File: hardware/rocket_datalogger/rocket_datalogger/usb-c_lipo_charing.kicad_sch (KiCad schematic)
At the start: 11 parts, among them J3 JST-PH 1x2, U3 MCP73831-2-OT

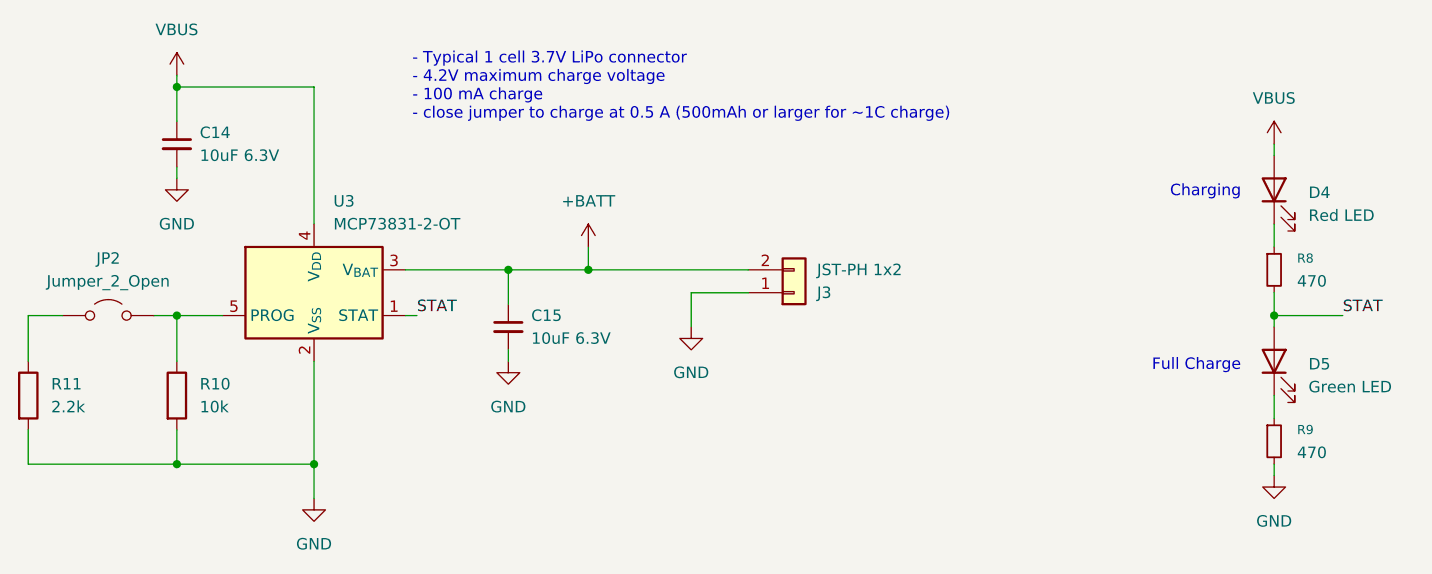
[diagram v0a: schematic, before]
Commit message: Changed IMU to BNO055
Previous IMU required 1.85V rail
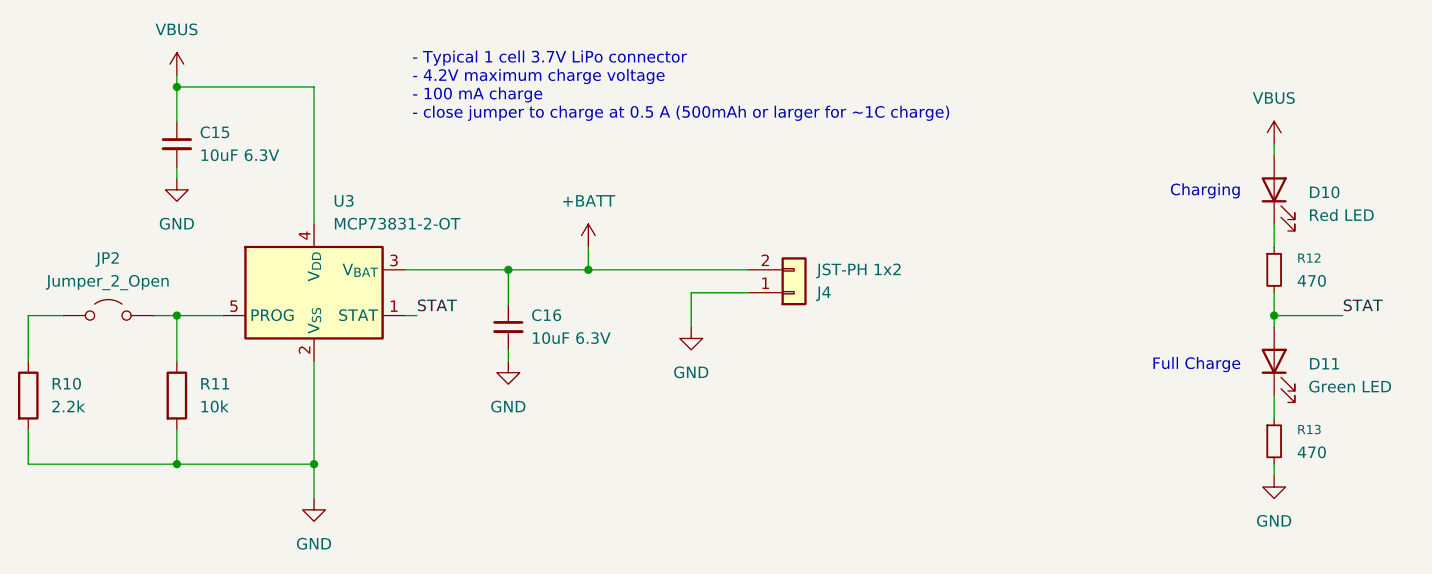
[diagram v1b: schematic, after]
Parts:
- renumbered C14 to C15, C15 to C16, D4 to D10, D5 to D11, J3 to J4, R11 to R10, R10 to R11, R8 to R12, R9 to R13
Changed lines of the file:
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@@
 		(dnp no)
 		(fields_autoplaced yes)
-		(property "Reference" "D5"
+		(property "Reference" "D11"
 			(at 180.34 71.4374 90)
 			(effects
@@
 			(project "rocket_datalogger"
 				(path "/742f64ac-c4d8-4561-a2a9-e0e3f6f67ce8/03492796-47b7-4899-82ad-a016c701f9cb"
-					(reference "D5")
+					(reference "D11")
 					(unit 1)
 				)
@@
 		(dnp no)
 		(fields_autoplaced yes)
-		(property "Reference" "R10"
+		(property "Reference" "R11"
 			(at 57.15 73.6599 0)
 			(effects
@@
 			(project ""
 				(path "/742f64ac-c4d8-4561-a2a9-e0e3f6f67ce8/03492796-47b7-4899-82ad-a016c701f9cb"
-					(reference "R10")
+					(reference "R11")
 					(unit 1)
 				)
@@
 		(dnp no)
 		(fields_autoplaced yes)
-		(property "Reference" "#PWR01"
+		(property "Reference" "#PWR038"
 			(at 100.33 62.23 0)
 			(effects
@@
 			(project ""
 				(path "/742f64ac-c4d8-4561-a2a9-e0e3f6f67ce8/03492796-47b7-4899-82ad-a016c701f9cb"
-					(reference "#PWR01")
+					(reference "#PWR038")
 					(unit 1)
 				)
@@
 		(dnp no)
 		(fields_autoplaced yes)
-		(property "Reference" "R9"
+		(property "Reference" "R13"
 			(at 179.07 78.7399 0)
 			(effects
@@
 			(project "rocket_datalogger"
 				(path "/742f64ac-c4d8-4561-a2a9-e0e3f6f67ce8/03492796-47b7-4899-82ad-a016c701f9cb"
-					(reference "R9")
+					(reference "R13")
 					(unit 1)
 				)
@@
 		(dnp no)
 		(fields_autoplaced yes)
-		(property "Reference" "#PWR031"
+		(property "Reference" "#PWR036"
 			(at 69.85 92.71 0)
 			(effects
@@
 			(project "rocket_datalogger"
 				(path "/742f64ac-c4d8-4561-a2a9-e0e3f6f67ce8/03492796-47b7-4899-82ad-a016c701f9cb"
-					(reference "#PWR031")
+					(reference "#PWR036")
 					(unit 1)
 				)
@@
 		(dnp no)
 		(fields_autoplaced yes)
-		(property "Reference" "R11"
+		(property "Reference" "R10"
 			(at 40.64 73.6599 0)
 			(effects
@@
 			(project "rocket_datalogger"
 				(path "/742f64ac-c4d8-4561-a2a9-e0e3f6f67ce8/03492796-47b7-4899-82ad-a016c701f9cb"
-					(reference "R11")
+					(reference "R10")
 					(unit 1)
 				)
@@
 		(dnp no)
 		(fields_autoplaced yes)
-		(property "Reference" "C14"
+		(property "Reference" "C15"
 			(at 57.15 45.7262 0)
 			(effects
@@
 			(project ""
 				(path "/742f64ac-c4d8-4561-a2a9-e0e3f6f67ce8/03492796-47b7-4899-82ad-a016c701f9cb"
-					(reference "C14")
+					(reference "C15")
 					(unit 1)
 				)
@@
 		(dnp no)
 		(fields_autoplaced yes)
-		(property "Reference" "R8"
+		(property "Reference" "R12"
 			(at 179.07 59.6899 0)
 			(effects
@@
 			(project ""
 				(path "/742f64ac-c4d8-4561-a2a9-e0e3f6f67ce8/03492796-47b7-4899-82ad-a016c701f9cb"
-					(reference "R8")
+					(reference "R12")
 					(unit 1)
 				)
@@
 		(dnp no)
 		(fields_autoplaced yes)
-		(property "Reference" "#PWR026"
+		(property "Reference" "#PWR034"
 			(at 54.61 43.18 0)
 			(effects
@@
 			(project "rocket_datalogger"
 				(path "/742f64ac-c4d8-4561-a2a9-e0e3f6f67ce8/03492796-47b7-4899-82ad-a016c701f9cb"
-					(reference "#PWR026")
+					(reference "#PWR034")
 					(unit 1)
 				)
@@
 		(dnp no)
 		(fields_autoplaced yes)
-		(property "Reference" "#PWR028"
+		(property "Reference" "#PWR040"
 			(at 176.53 50.8 0)
 			(effects
@@
 			(project "rocket_datalogger"
 				(path "/742f64ac-c4d8-4561-a2a9-e0e3f6f67ce8/03492796-47b7-4899-82ad-a016c701f9cb"
-					(reference "#PWR028")
+					(reference "#PWR040")
 					(unit 1)
 				)
@@
 		(dnp no)
 		(fields_autoplaced yes)
-		(property "Reference" "#PWR030"
+		(property "Reference" "#PWR037"
 			(at 91.44 77.47 0)
 			(effects
@@
 			(project "rocket_datalogger"
 				(path "/742f64ac-c4d8-4561-a2a9-e0e3f6f67ce8/03492796-47b7-4899-82ad-a016c701f9cb"
-					(reference "#PWR030")
+					(reference "#PWR037")
 					(unit 1)
 				)
@@
 		(dnp no)
 		(fields_autoplaced yes)
-		(property "Reference" "D4"
+		(property "Reference" "D10"
 			(at 180.34 52.3874 90)
 			(effects
@@
 			(project ""
 				(path "/742f64ac-c4d8-4561-a2a9-e0e3f6f67ce8/03492796-47b7-4899-82ad-a016c701f9cb"
-					(reference "D4")
+					(reference "D10")
 					(unit 1)
 				)
@@
 		(dnp no)
 		(fields_autoplaced yes)
-		(property "Reference" "C15"
+		(property "Reference" "C16"
 			(at 93.98 66.0462 0)
 			(effects
@@
 			(project "rocket_datalogger"
 				(path "/742f64ac-c4d8-4561-a2a9-e0e3f6f67ce8/03492796-47b7-4899-82ad-a016c701f9cb"
-					(reference "C15")
+					(reference "C16")
 					(unit 1)
 				)
@@
 		(dnp no)
 		(fields_autoplaced yes)
-		(property "Reference" "#PWR025"
+		(property "Reference" "#PWR041"
 			(at 176.53 90.17 0)
 			(effects
@@
 			(project "rocket_datalogger"
 				(path "/742f64ac-c4d8-4561-a2a9-e0e3f6f67ce8/03492796-47b7-4899-82ad-a016c701f9cb"
-					(reference "#PWR025")
+					(reference "#PWR041")
 					(unit 1)
 				)
@@
 		(dnp no)
 		(fields_autoplaced yes)
-		(property "Reference" "#PWR029"
+		(property "Reference" "#PWR039"
 			(at 111.76 73.66 0)
 			(effects
@@
 			(project "rocket_datalogger"
 				(path "/742f64ac-c4d8-4561-a2a9-e0e3f6f67ce8/03492796-47b7-4899-82ad-a016c701f9cb"
-					(reference "#PWR029")
+					(reference "#PWR039")
 					(unit 1)
 				)
@@
 		(on_board yes)
 		(dnp no)
-		(property "Reference" "J3"
+		(property "Reference" "J4"
 			(at 125.73 63.5001 0)
 			(effects
@@
 			(project ""
 				(path "/742f64ac-c4d8-4561-a2a9-e0e3f6f67ce8/03492796-47b7-4899-82ad-a016c701f9cb"
-					(reference "J3")
+					(reference "J4")
 					(unit 1)
 				)
@@
 		(dnp no)
 		(fields_autoplaced yes)
-		(property "Reference" "#PWR027"
+		(property "Reference" "#PWR035"
 			(at 54.61 57.15 0)
 			(effects
@@
 			(project ""
 				(path "/742f64ac-c4d8-4561-a2a9-e0e3f6f67ce8/03492796-47b7-4899-82ad-a016c701f9cb"
-					(reference "#PWR027")
-					(unit 1)
-				)
+					(reference "#PWR035")
+					(unit 1)
+				)

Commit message: fixed minor hardware issues
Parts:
- C15, C16: footprint (none) -> Capacitor_SMD:C_0603_1608Metric
- D10, D11: footprint (none) -> LED_SMD:LED_0603_1608Metric
- R10, R11, R12, R13: footprint (none) -> Resistor_SMD:R_0603_1608Metric
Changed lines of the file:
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@@
 			)
 		)
-		(property "Footprint" ""
+		(property "Footprint" "LED_SMD:LED_0603_1608Metric"
 			(at 176.53 71.12 0)
 			(effects
@@
 			)
 		)
-		(property "Footprint" ""
+		(property "Footprint" "Resistor_SMD:R_0603_1608Metric"
 			(at 52.832 74.93 90)
 			(effects
@@
 			)
 		)
-		(property "Footprint" ""
+		(property "Footprint" "Resistor_SMD:R_0603_1608Metric"
 			(at 176.53 80.01 0)
 			(effects
@@
 			)
 		)
-		(property "Footprint" ""
+		(property "Footprint" "Resistor_SMD:R_0603_1608Metric"
 			(at 36.322 74.93 90)
 			(effects
@@
 			)
 		)
-		(property "Footprint" ""
+		(property "Footprint" "Capacitor_SMD:C_0603_1608Metric"
 			(at 54.61 46.99 0)
 			(effects
@@
 			)
 		)
-		(property "Footprint" ""
+		(property "Footprint" "Resistor_SMD:R_0603_1608Metric"
 			(at 176.53 60.96 0)
 			(effects
@@
 			)
 		)
-		(property "Footprint" ""
+		(property "Footprint" "LED_SMD:LED_0603_1608Metric"
 			(at 176.53 52.07 0)
 			(effects
@@
 			)
 		)
-		(property "Footprint" ""
+		(property "Footprint" "Capacitor_SMD:C_0603_1608Metric"
 			(at 91.44 67.31 0)
 			(effects

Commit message: Minor revision
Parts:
- J4: footprint (none) -> Connector_JST:JST_PH_S2B-PH-K_1x02_P2.00mm_Horizontal
- JP2: footprint (none) -> Jumper:SolderJumper-2_P1.3mm_Open_RoundedPad1.0x1.5mm
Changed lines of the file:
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@@
 			)
 		)
-		(property "Footprint" ""
+		(property "Footprint" "Jumper:SolderJumper-2_P1.3mm_Open_RoundedPad1.0x1.5mm"
 			(at 46.99 66.04 0)
 			(effects
@@
 			)
 		)
-		(property "Footprint" ""
+		(property "Footprint" "Connector_JST:JST_PH_S2B-PH-K_1x02_P2.00mm_Horizontal"
 			(at 123.19 63.5 0)
 			(effects
